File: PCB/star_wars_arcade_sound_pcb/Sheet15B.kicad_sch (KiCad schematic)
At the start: 19 parts

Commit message: Began PCB layout
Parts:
- E_1: footprint (none) -> atari:DDIP40
- J/K_1: footprint (none) -> atari:DIP28
- J_2, J_3: footprint (none) -> atari:DIP16
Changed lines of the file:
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@@
     (property "Reference" "J_3" (id 0) (at 60.96 125.095 0))
     (property "Value" "74LS139" (id 1) (at 62.23 142.24 0))
-    (property "Footprint" "" (id 2) (at 57.785 133.35 0)
+    (property "Footprint" "atari:DIP16" (id 2) (at 57.785 133.35 0)
       (effects (font (size 1.27 1.27)) hide)
     )
@@
       (effects (font (size 1.27 1.27)) (justify left))
     )
-    (property "Footprint" "" (id 2) (at 60.325 55.88 0)
+    (property "Footprint" "atari:DIP16" (id 2) (at 60.325 55.88 0)
       (effects (font (size 1.27 1.27)) hide)
     )
@@
       (effects (font (size 1.27 1.27)) (justify left))
     )
-    (property "Footprint" "" (id 2) (at 57.785 133.35 0)
+    (property "Footprint" "atari:DIP16" (id 2) (at 57.785 133.35 0)
       (effects (font (size 1.27 1.27)) hide)
     )
@@
       (effects (font (size 1.27 1.27)) (justify left))
     )
-    (property "Footprint" "" (id 2) (at 124.46 134.62 0)
+    (property "Footprint" "atari:DDIP40" (id 2) (at 124.46 134.62 0)
       (effects (font (size 1.27 1.27)) hide)
     )
@@
     (property "Reference" "J_2" (id 0) (at 60.325 31.115 0))
     (property "Value" "74LS139" (id 1) (at 59.69 28.575 0))
-    (property "Footprint" "" (id 2) (at 60.325 29.845 0)
+    (property "Footprint" "atari:DIP16" (id 2) (at 60.325 29.845 0)
       (effects (font (size 1.27 1.27)) hide)
     )
@@
     (property "Reference" "J_2" (id 0) (at 60.325 58.42 0))
     (property "Value" "74LS139" (id 1) (at 59.69 55.88 0))
-    (property "Footprint" "" (id 2) (at 60.325 55.88 0)
+    (property "Footprint" "atari:DIP16" (id 2) (at 60.325 55.88 0)
       (effects (font (size 1.27 1.27)) hide)
     )
@@
       (effects (font (size 1.27 1.27)) (justify left))
     )
-    (property "Footprint" "" (id 2) (at 159.385 54.61 0)
-      (effects (font (size 1.27 1.27)) hide)
-    )
+    (property "Footprint" "atari:DIP28" (id 2) (at 159.385 54.61 0)
+      (effects (font (size 1.27 1.27)) hide)
+    )

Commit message: ICs placed
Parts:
- F/H_1: footprint (none) -> atari:DDIP24
- H_1: footprint (none) -> atari:DIP28
- H_2, H_3: footprint (none) -> atari:DIP14
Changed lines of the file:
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@@
     (property "Reference" "H_3" (id 0) (at 67.945 99.695 0))
     (property "Value" "74LS00" (id 1) (at 64.77 103.505 0))
-    (property "Footprint" "" (id 2) (at 62.23 94.615 0)
+    (property "Footprint" "atari:DIP14" (id 2) (at 62.23 94.615 0)
       (effects (font (size 1.27 1.27)) hide)
     )
@@
       (effects (font (size 1.27 1.27)) (justify left))
     )
-    (property "Footprint" "" (id 2) (at 120.015 54.61 0)
+    (property "Footprint" "atari:DIP28" (id 2) (at 120.015 54.61 0)
       (effects (font (size 1.27 1.27)) hide)
     )
@@
     (property "Reference" "H_3" (id 0) (at 232.41 102.235 0))
     (property "Value" "74LS00" (id 1) (at 233.045 100.33 0))
-    (property "Footprint" "" (id 2) (at 233.045 100.965 0)
+    (property "Footprint" "atari:DIP14" (id 2) (at 233.045 100.965 0)
       (effects (font (size 1.27 1.27)) hide)
     )
@@
       (effects (font (size 1.27 1.27)) (justify left))
     )
-    (property "Footprint" "" (id 2) (at 41.91 97.155 0)
+    (property "Footprint" "atari:DIP14" (id 2) (at 41.91 97.155 0)
       (effects (font (size 1.27 1.27)) hide)
     )
@@
     (property "Reference" "H_2" (id 0) (at 46.355 99.06 0))
     (property "Value" "74LS04" (id 1) (at 46.99 94.615 0))
-    (property "Footprint" "" (id 2) (at 41.275 97.155 0)
+    (property "Footprint" "atari:DIP14" (id 2) (at 41.275 97.155 0)
       (effects (font (size 1.27 1.27)) hide)
     )
@@
       (effects (font (size 1.27 1.27)) (justify left))
     )
-    (property "Footprint" "" (id 2) (at 60.325 94.615 0)
+    (property "Footprint" "atari:DIP14" (id 2) (at 60.325 94.615 0)
       (effects (font (size 1.27 1.27)) hide)
     )
@@
       (effects (font (size 1.27 1.27)) (justify left))
     )
-    (property "Footprint" "" (id 2) (at 240.03 94.615 0)
+    (property "Footprint" "atari:DDIP24" (id 2) (at 240.03 94.615 0)
       (effects (font (size 1.27 1.27)) hide)
     )
@@
     (property "Reference" "H_2" (id 0) (at 210.82 118.11 0))
     (property "Value" "74LS04" (id 1) (at 212.09 123.19 0))
-    (property "Footprint" "" (id 2) (at 207.645 120.65 0)
-      (effects (font (size 1.27 1.27)) hide)
-    )
+    (property "Footprint" "atari:DIP14" (id 2) (at 207.645 120.65 0)
+      (effects (font (size 1.27 1.27)) hide)
+    )

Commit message: Placed all components
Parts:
- C10, C11, C2, C20, C3, C4, C5, C7, R5, R6: footprint (none) -> atari:GenericComp
- TP7: footprint (none) -> atari:TEST_POINT
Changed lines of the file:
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@@
     (property "Reference" "C5" (id 0) (at 136.525 107.95 90))
     (property "Value" ".1uf" (id 1) (at 136.525 105.41 90))
-    (property "Footprint" "" (id 2) (at 137.16 105.7148 0)
+    (property "Footprint" "atari:GenericComp" (id 2) (at 137.16 105.7148 0)
       (effects (font (size 1.27 1.27)) hide)
     )
@@
       (effects (font (size 1.27 1.27)) (justify left))
     )
-    (property "Footprint" "" (id 2) (at 157.226 169.799 90)
+    (property "Footprint" "atari:GenericComp" (id 2) (at 157.226 169.799 90)
       (effects (font (size 1.27 1.27)) hide)
     )
@@
       (effects (font (size 1.27 1.27)) (justify left))
     )
-    (property "Footprint" "" (id 2) (at 159.766 152.654 90)
+    (property "Footprint" "atari:GenericComp" (id 2) (at 159.766 152.654 90)
       (effects (font (size 1.27 1.27)) hide)
     )
@@
     (property "Reference" "C3" (id 0) (at 132.715 27.94 90))
     (property "Value" ".1uf" (id 1) (at 133.35 25.4 90))
-    (property "Footprint" "" (id 2) (at 133.985 25.7048 0)
+    (property "Footprint" "atari:GenericComp" (id 2) (at 133.985 25.7048 0)
       (effects (font (size 1.27 1.27)) hide)
     )
@@
     (property "Reference" "C2" (id 0) (at 172.085 27.94 90))
     (property "Value" ".1uf" (id 1) (at 172.72 25.4 90))
-    (property "Footprint" "" (id 2) (at 173.355 25.7048 0)
+    (property "Footprint" "atari:GenericComp" (id 2) (at 173.355 25.7048 0)
       (effects (font (size 1.27 1.27)) hide)
     )
@@
     (property "Reference" "C10" (id 0) (at 33.02 86.995 90))
     (property "Value" ".1uf" (id 1) (at 33.02 89.535 90))
-    (property "Footprint" "" (id 2) (at 32.385 89.2302 0)
+    (property "Footprint" "atari:GenericComp" (id 2) (at 32.385 89.2302 0)
       (effects (font (size 1.27 1.27)) hide)
     )
@@
     (property "Reference" "C4" (id 0) (at 260.985 60.96 90))
     (property "Value" ".1uf" (id 1) (at 261.62 58.42 90))
-    (property "Footprint" "" (id 2) (at 262.255 58.7248 0)
+    (property "Footprint" "atari:GenericComp" (id 2) (at 262.255 58.7248 0)
       (effects (font (size 1.27 1.27)) hide)
     )
@@
     (property "Reference" "C7" (id 0) (at 68.58 45.72 90))
     (property "Value" ".1uf" (id 1) (at 69.215 43.18 90))
-    (property "Footprint" "" (id 2) (at 69.85 43.4848 0)
+    (property "Footprint" "atari:GenericComp" (id 2) (at 69.85 43.4848 0)
       (effects (font (size 1.27 1.27)) hide)
     )
@@
     (property "Reference" "C11" (id 0) (at 68.58 85.09 90))
     (property "Value" ".1uf" (id 1) (at 68.58 82.55 90))
-    (property "Footprint" "" (id 2) (at 69.215 82.8548 0)
+    (property "Footprint" "atari:GenericComp" (id 2) (at 69.215 82.8548 0)
       (effects (font (size 1.27 1.27)) hide)
     )
@@
       (effects (font (size 1.27 1.27)) (justify left) hide)
     )
-    (property "Footprint" "" (id 2) (at 167.005 157.48 0)
+    (property "Footprint" "atari:TEST_POINT" (id 2) (at 167.005 157.48 0)
       (effects (font (size 1.27 1.27)) hide)
     )
@@
     (property "Reference" "C20" (id 0) (at 66.04 122.555 90))
     (property "Value" ".1uf" (id 1) (at 66.04 120.015 90))
-    (property "Footprint" "" (id 2) (at 66.675 120.3198 0)
-      (effects (font (size 1.27 1.27)) hide)
-    )
+    (property "Footprint" "atari:GenericComp" (id 2) (at 66.675 120.3198 0)
+      (effects (font (size 1.27 1.27)) hide)
+    )

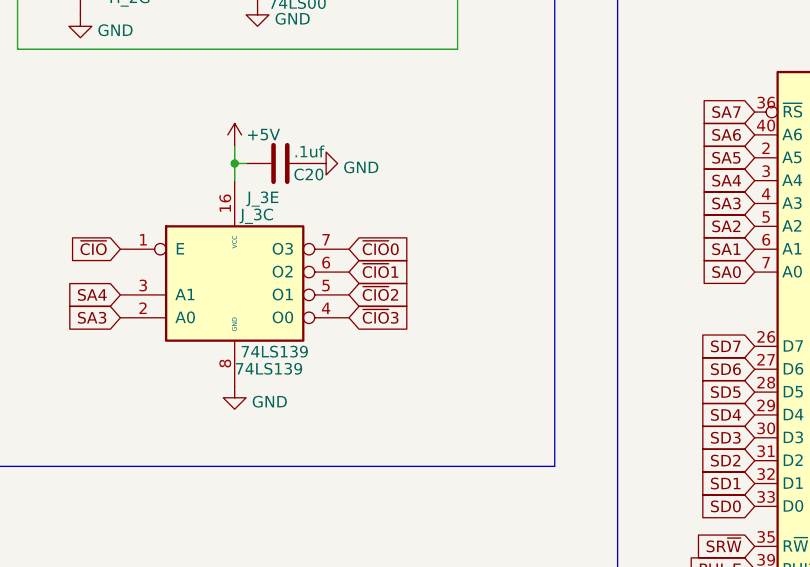
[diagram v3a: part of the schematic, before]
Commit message: 374 connections remain
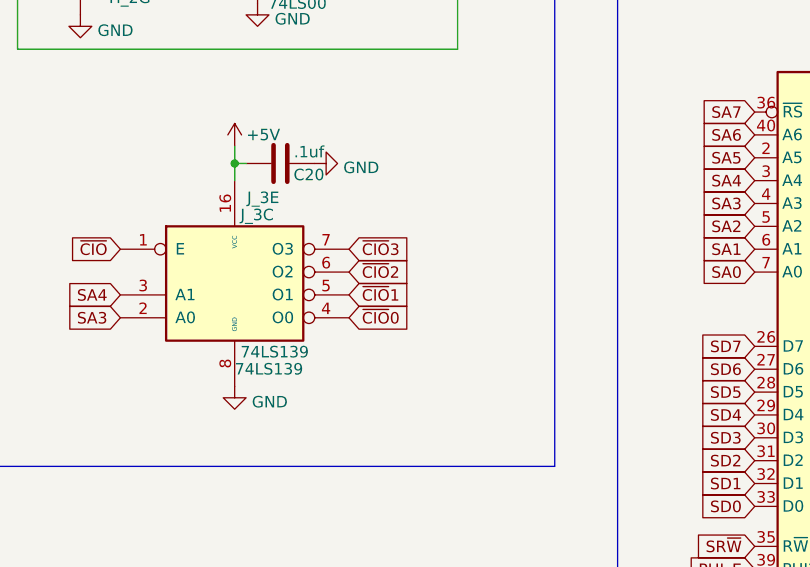
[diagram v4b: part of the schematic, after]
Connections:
- net ~{CIO}0: now also J_3.4 (O0); no longer J_3.7 (O3)
- net ~{CIO}1: now also J_3.5 (O1); no longer J_3.6 (O2)
- net ~{CIO}2: now also J_3.6 (O2); no longer J_3.5 (O1)
- net ~{CIO}3: now also J_3.7 (O3); no longer J_3.4 (O0)
